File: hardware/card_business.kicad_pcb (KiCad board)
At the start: 2 copper layers, 49.9 x 17.3 mm, 12 parts, among them J1 Conn_01x01_Female, J2 USB_A, SW1 Reset, SW2 Boot, U1 CH552G

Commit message: Change pin name and routing update
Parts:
- SW1, SW2: footprint Connectors:C455281 -> Button_Switch_SMD:SW_SPST_TL3342
- moved R1 15.0 mm to (105.1, 95.5)
- moved R3 14.1 mm to (95.8, 92.8)
- moved SW1 13.2 mm to (114.1, 93.7), turned to 0 degrees
- moved D1 8.54 mm to (95.9, 88.0), turned to 180 degrees
- moved J2 6.96 mm to (79.5, 86.0)
- moved U1 6.13 mm to (104.2, 85.5)
- moved J1 5.32 mm to (136.5, 92.5)
- moved R2 5.28 mm to (111.1, 87.2)
- moved SW2 4.50 mm to (123.2, 93.7), turned to 0 degrees
- moved C1 3.46 mm to (98.0, 81.0)
- moved C2 3.25 mm to (98.0, 78.8)
- moved G*** 2.25 mm to (130.5, 81.0)
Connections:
- net /UDM renamed /UD-
- net /UDP renamed /UD+
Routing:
- net +5V: track 49.8 -> 64.0 mm, vias 2 -> 1
- net /PAD: track 27.0 -> 38.5 mm
- net GND: track 43.6 -> 33.2 mm, vias 2 -> 1
- net Net-(R2-Pad1): track 9.01 -> 17.9 mm
- net /RST: track 2.25 -> 10.9 mm
- net /UD-: track 24.9 -> 20.0 mm
- net /UD+: track 28.5 -> 30.2 mm, vias 3 -> 1
- net /P3.3: track 7.80 -> 6.74 mm
- net Net-(R1-Pad2): track 12.2 -> 11.3 mm
- net Net-(D1-Pad2): track 5.48 -> 4.78 mm
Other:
- board size 49.9 x 17.3 mm -> 62 x 22.5 mm

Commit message: update labels
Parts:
- renumbered SW2 to BOOT, D1 to LED, SW1 to RST, J1 to TOUCHME
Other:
- board text added: "Phone: 4491101599"
- board text removed: "Phone: XXXXXXXXXX"

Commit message: add back labels
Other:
- board text added: "Instructions: 1.- Plug into USB port 2.- Wait for device to be ready 3.- Open your favorite tex editor 4.- Press Caps Lock three times 5.- Watch the magic!"

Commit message: update traces v1.0
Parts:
- turned BOOT to 180 degrees
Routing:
- net Net-(R2-Pad1): track 17.9 -> 27.6 mm
- net +5V: track 64.0 -> 72.3 mm
- net Net-(D1-Pad2): track 4.78 -> 8.39 mm
- net /PAD: track 38.5 -> 39.2 mm
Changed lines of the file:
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@@
-(kicad_pcb (version 20171130) (host pcbnew "(5.1.9)-1")
+(kicad_pcb (version 20171130) (host pcbnew "(5.1.5-0-10_14)")
   (general
     (thickness 1.6)
     (drawings 21)
-    (tracks 100)
+    (tracks 112)
     (zones 0)
     (modules 12)
@@
   )
   (setup
-    (last_trace_width 0.25)
+    (last_trace_width 0.3)
+    (user_trace_width 0.3)
+    (user_trace_width 0.5)
     (trace_clearance 0.2)
     (zone_clearance 0.508)
@@
   )
   (module Button_Switch_SMD:SW_SPST_TL3342 (layer F.Cu)
-    (at 123.15 93.65)
+    (at 123.15 93.65 180)
     (descr "Low-profile SMD Tactile Switch, https://www.e-switch.com/system/asset/product_line/data_sheet/165/TL3342.pdf")
     (tags "SPST Tactile Switch")
@@
       (effects (font (size 1 1) (thickness 0.15)))
     )
-    (pad 2 smd rect (at 3.15 1.9) (size 1.7 1) (layers F.Cu F.Paste F.Mask)
+    (pad 2 smd rect (at 3.15 1.9 180) (size 1.7 1) (layers F.Cu F.Paste F.Mask)
       (net 1 +5V))
-    (pad 2 smd rect (at -3.15 1.9) (size 1.7 1) (layers F.Cu F.Paste F.Mask)
+    (pad 2 smd rect (at -3.15 1.9 180) (size 1.7 1) (layers F.Cu F.Paste F.Mask)
       (net 1 +5V))
-    (pad 1 smd rect (at 3.15 -1.9) (size 1.7 1) (layers F.Cu F.Paste F.Mask)
+    (pad 1 smd rect (at 3.15 -1.9 180) (size 1.7 1) (layers F.Cu F.Paste F.Mask)
       (net 7 "Net-(R2-Pad1)"))
-    (pad 1 smd rect (at -3.15 -1.9) (size 1.7 1) (layers F.Cu F.Paste F.Mask)
+    (pad 1 smd rect (at -3.15 -1.9 180) (size 1.7 1) (layers F.Cu F.Paste F.Mask)
       (net 7 "Net-(R2-Pad1)"))
     (model ${KISYS3DMOD}/Button_Switch_SMD.3dshapes/SW_SPST_TL3342.wrl
@@
     (effects (font (size 2 2) (thickness 0.3)))
   )
-  (segment (start 99 78.75) (end 99 81) (width 0.3) (layer B.Cu) (net 1))
   (segment (start 99 81) (end 99 82) (width 0.3) (layer B.Cu) (net 1))
   (segment (start 99.325 82.325) (end 101 82.325) (width 0.3) (layer B.Cu) (net 1))
   (segment (start 99 82) (end 99.325 82.325) (width 0.3) (layer B.Cu) (net 1))
-  (via (at 103.5 85) (size 0.8) (drill 0.4) (layers F.Cu B.Cu) (net 1))
-  (segment (start 103.5 84.025) (end 103.5 85) (width 0.3) (layer B.Cu) (net 1))
-  (segment (start 101.8 82.325) (end 103.5 84.025) (width 0.3) (layer B.Cu) (net 1))
-  (segment (start 101 82.325) (end 101.8 82.325) (width 0.3) (layer B.Cu) (net 1))
-  (segment (start 120 95.55) (end 119.55 95.55) (width 0.3) (layer F.Cu) (net 1))
-  (segment (start 126.3 95.55) (end 120 95.55) (width 0.3) (layer F.Cu) (net 1))
-  (segment (start 120 95.55) (end 120 94.5) (width 0.3) (layer F.Cu) (net 1))
-  (segment (start 120 94.5) (end 119.25 93.75) (width 0.3) (layer F.Cu) (net 1))
-  (segment (start 119.25 93.75) (end 117.75 93.75) (width 0.3) (layer F.Cu) (net 1))
-  (segment (start 117.25 93.25) (end 117.25 91.75) (width 0.3) (layer F.Cu) (net 1))
-  (segment (start 117.75 93.75) (end 117.25 93.25) (width 0.3) (layer F.Cu) (net 1))
-  (segment (start 117.25 91.75) (end 110.95 91.75) (width 0.3) (layer F.Cu) (net 1))
-  (segment (start 103.5 85) (end 103.5 90.5) (width 0.3) (layer F.Cu) (net 1))
-  (segment (start 104.75 91.75) (end 110.95 91.75) (width 0.3) (layer F.Cu) (net 1))
-  (segment (start 84.4 89.81) (end 92.31 89.81) (width 0.3) (layer F.Cu) (net 1))
-  (segment (start 92.31 89.81) (end 93 90.5) (width 0.3) (layer F.Cu) (net 1))
-  (segment (start 93 90.5) (end 93 91.75) (width 0.3) (layer F.Cu) (net 1))
-  (segment (start 93 91.75) (end 94 92.75) (width 0.3) (layer F.Cu) (net 1))
-  (segment (start 101.5 92.75) (end 103.625 90.625) (width 0.3) (layer F.Cu) (net 1))
-  (segment (start 94 92.75) (end 101.5 92.75) (width 0.3) (layer F.Cu) (net 1))
-  (segment (start 103.625 90.625) (end 104.75 91.75) (width 0.3) (layer F.Cu) (net 1))
-  (segment (start 103.5 90.5) (end 103.625 90.625) (width 0.3) (layer F.Cu) (net 1))
+  (segment (start 120 95.55) (end 119.55 95.55) (width 0.3) (layer F.Cu) (net 7))
+  (segment (start 99 81) (end 99 78.75) (width 0.5) (layer B.Cu) (net 1))
+  (via (at 103.71 78.6) (size 0.8) (drill 0.4) (layers F.Cu B.Cu) (net 1))
+  (segment (start 103.56 78.75) (end 103.71 78.6) (width 0.5) (layer B.Cu) (net 1))
+  (segment (start 99 78.75) (end 103.56 78.75) (width 0.5) (layer B.Cu) (net 1))
+  (segment (start 92.858 89.81) (end 84.4 89.81) (width 0.5) (layer F.Cu) (net 1))
+  (segment (start 94.798 91.75) (end 92.858 89.81) (width 0.5) (layer F.Cu) (net 1))
+  (segment (start 103.688 91.75) (end 103.71 91.728) (width 0.5) (layer F.Cu) (net 1))
+  (segment (start 103.71 90.7) (end 103.71 91) (width 0.5) (layer F.Cu) (net 1))
+  (segment (start 103.71 91) (end 102.94 91.77) (width 0.5) (layer F.Cu) (net 1))
+  (segment (start 103.688 91.75) (end 102.94 91.77) (width 0.5) (layer F.Cu) (net 1))
+  (segment (start 102.94 91.77) (end 94.798 91.75) (width 0.5) (layer F.Cu) (net 1))
+  (segment (start 103.71 90.7) (end 103.71 78.6) (width 0.5) (layer F.Cu) (net 1))
+  (segment (start 103.71 91.04) (end 103.71 91.26) (width 0.5) (layer F.Cu) (net 1))
+  (segment (start 104.22 91.77) (end 103.688 91.75) (width 0.5) (layer F.Cu) (net 1))
+  (segment (start 103.71 91.26) (end 104.22 91.77) (width 0.5) (layer F.Cu) (net 1))
+  (segment (start 103.71 91.728) (end 103.71 91.04) (width 0.5) (layer F.Cu) (net 1))
+  (segment (start 103.71 91.04) (end 103.71 90.7) (width 0.5) (layer F.Cu) (net 1))
+  (segment (start 104.477838 91.767838) (end 103.71 91) (width 0.5) (layer F.Cu) (net 1))
+  (segment (start 104.947838 91.767838) (end 104.477838 91.767838) (width 0.5) (layer F.Cu) (net 1))
+  (segment (start 110.95 91.75) (end 104.947838 91.767838) (width 0.5) (layer F.Cu) (net 1))
+  (segment (start 104.947838 91.767838) (end 104.22 91.77) (width 0.5) (layer F.Cu) (net 1))
+  (segment (start 117.25 91.75) (end 110.95 91.75) (width 0.5) (layer F.Cu) (net 1))
+  (segment (start 119.39999 91.75) (end 119.39999 91.998532) (width 0.5) (layer F.Cu) (net 1))
+  (segment (start 117.25 91.75) (end 119.39999 91.75) (width 0.5) (layer F.Cu) (net 1))
   (segment (start 97.1 78.75) (end 97.1 81) (width 0.3) (layer B.Cu) (net 2))
   (segment (start 97.1 81) (end 97.1 82.85) (width 0.3) (layer B.Cu) (net 2))
@@
   (segment (start 98 86.875) (end 98 82.75) (width 0.3) (layer F.Cu) (net 2))
   (segment (start 96.875 88) (end 98 86.875) (width 0.3) (layer F.Cu) (net 2))
-  (via (at 95 90.75) (size 0.8) (drill 0.4) (layers F.Cu B.Cu) (net 3))
-  (segment (start 94.925 90.825) (end 95 90.75) (width 0.3) (layer B.Cu) (net 3))
-  (segment (start 94.925 92.75) (end 94.925 90.825) (width 0.3) (layer B.Cu) (net 3))
-  (segment (start 95 90.75) (end 95 88) (width 0.3) (layer F.Cu) (net 3))
-  (via (at 135.75 82.75) (size 0.8) (drill 0.4) (layers F.Cu B.Cu) (net 4))
-  (segment (start 136.5 83.5) (end 135.75 82.75) (width 0.3) (layer F.Cu) (net 4))
-  (segment (start 136.5 92.5) (end 136.5 83.5) (width 0.3) (layer F.Cu) (net 4))
-  (segment (start 135.325 82.325) (end 107.5 82.325) (width 0.3) (layer B.Cu) (net 4))
-  (segment (start 135.75 82.75) (end 135.325 82.325) (width 0.3) (layer B.Cu) (net 4))
+  (via (at 93.01 87.95) (size 0.8) (drill 0.4) (layers F.Cu B.Cu) (net 3))
+  (segment (start 95 88) (end 93.06 88) (width 0.3) (layer F.Cu) (net 3))
+  (segment (start 93.06 88) (end 93.01 87.95) (width 0.3) (layer F.Cu) (net 3))
+  (segment (start 94.35 87.95) (end 93.01 87.95) (width 0.3) (layer B.Cu) (net 3))
+  (segment (start 94.925 88.525) (end 94.35 87.95) (width 0.3) (layer B.Cu) (net 3))
+  (segment (start 94.925 92.75) (end 94.925 88.525) (width 0.3) (layer B.Cu) (net 3))
   (segment (start 117.25 95.55) (end 110.95 95.55) (width 0.3) (layer F.Cu) (net 5))
   (via (at 108.5 95.5) (size 0.8) (drill 0.4) (layers F.Cu B.Cu) (net 5))
@@
   (segment (start 105.095 87.405) (end 107.5 87.405) (width 0.3) (layer B.Cu) (net 6))
   (segment (start 104.175 88.325) (end 105.095 87.405) (width 0.3) (layer B.Cu) (net 6))
-  (segment (start 126.3 91.75) (end 120 91.75) (width 0.3) (layer F.Cu) (net 7))
-  (via (at 118.75 87.5) (size 0.8) (drill 0.4) (layers F.Cu B.Cu) (net 7))
-  (segment (start 120 88.75) (end 118.75 87.5) (width 0.3) (layer F.Cu) (net 7))
-  (segment (start 120 91.75) (end 120 88.75) (width 0.3) (layer F.Cu) (net 7))
+  (segment (start 117.25 91.75) (end 120 91.75) (width 0.5) (layer F.Cu) (net 1))
+  (segment (start 121.35 91.75) (end 126.3 91.75) (width 0.5) (layer F.Cu) (net 1))
+  (segment (start 120 91.75) (end 121.35 91.75) (width 0.5) (layer F.Cu) (net 1))
+  (via (at 136.49 82.32) (size 0.8) (drill 0.4) (layers F.Cu B.Cu) (net 4))
+  (segment (start 136.485 82.325) (end 136.49 82.32) (width 0.3) (layer B.Cu) (net 4))
+  (segment (start 125.965 82.325) (end 136.485 82.325) (width 0.3) (layer B.Cu) (net 4))
+  (segment (start 125.965 82.325) (end 107.5 82.325) (width 0.3) (layer B.Cu) (net 4))
+  (segment (start 136.49 92.49) (end 136.5 92.5) (width 0.3) (layer F.Cu) (net 4))
+  (segment (start 136.49 82.32) (end 136.49 92.49) (width 0.3) (layer F.Cu) (net 4))
   (segment (start 112.25 87.5) (end 112 87.25) (width 0.3) (layer B.Cu) (net 7))
-  (segment (start 118.75 87.5) (end 112.25 87.5) (width 0.3) (layer B.Cu) (net 7))
+  (segment (start 126.3 95.55) (end 128.62 95.55) (width 0.3) (layer F.Cu) (net 7))
+  (segment (start 128.62 95.55) (end 129.32 94.85) (width 0.3) (layer F.Cu) (net 7))
+  (segment (start 115.87 87.5) (end 121.16 87.5) (width 0.3) (layer B.Cu) (net 7))
+  (segment (start 115.87 87.5) (end 112.25 87.5) (width 0.3) (layer B.Cu) (net 7))
+  (segment (start 121.16 87.5) (end 121.85 88.19) (width 0.3) (layer B.Cu) (net 7))
+  (via (at 121.85 95.45) (size 0.8) (drill 0.4) (layers F.Cu B.Cu) (net 7))
+  (segment (start 121.85 88.19) (end 121.85 95.45) (width 0.3) (layer B.Cu) (net 7))
+  (segment (start 121.85 95.45) (end 126.3 95.55) (width 0.5) (layer F.Cu) (net 7))
+  (segment (start 120 95.55) (end 121.85 95.45) (width 0.5) (layer F.Cu) (net 7))
   (segment (start 96.75 92.75) (end 97.5 92.75) (width 0.25) (layer B.Cu) (net 8))
   (segment (start 97.5 92.75) (end 99 91.25) (width 0.25) (layer B.Cu) (net 8))

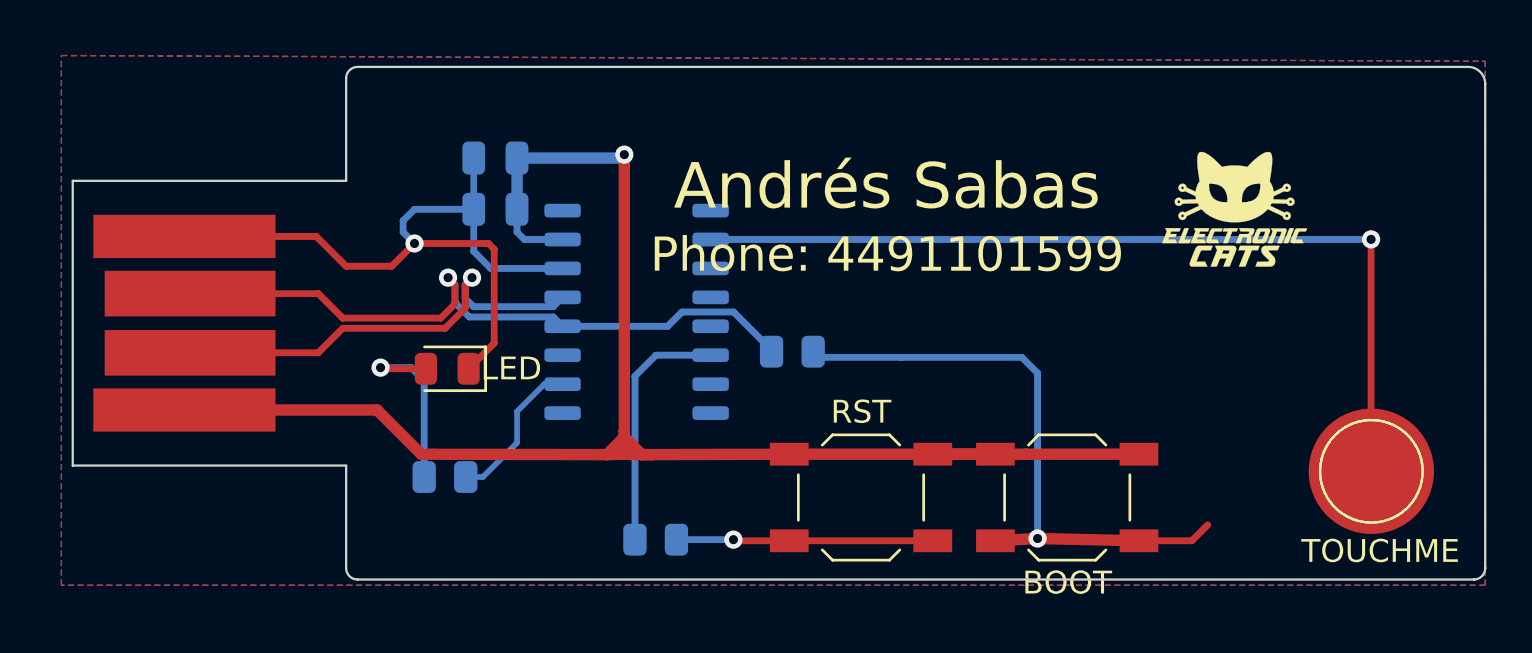
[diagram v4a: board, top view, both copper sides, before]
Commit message: add capacitor, modify traces
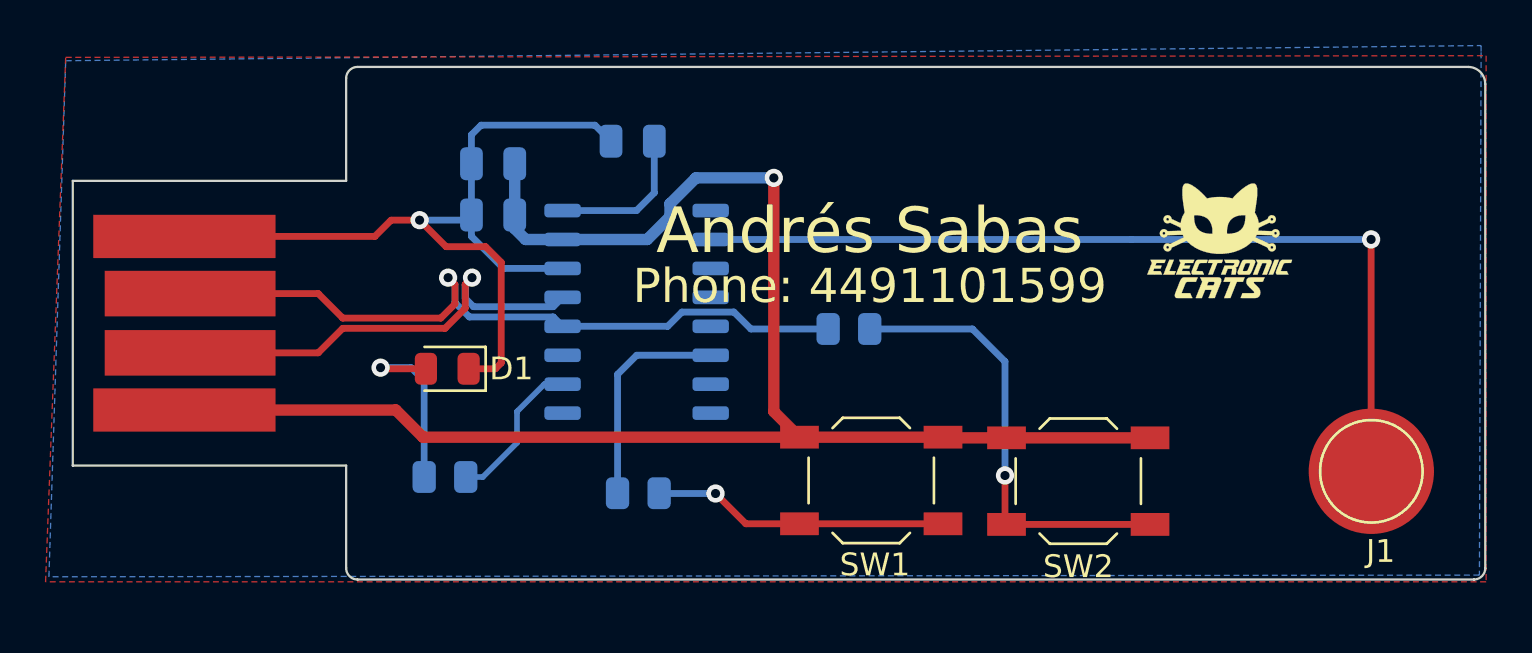
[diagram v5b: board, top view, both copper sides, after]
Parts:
- added C3: 0.1uF, Capacitor_SMD:C_0805_2012Metric, B.Cu at (104.1, 78.0)
- moved R2 2.67 mm to (113.6, 86.3)
- moved R1 2.18 mm to (104.3, 93.5)
- moved G*** 1.53 mm to (129.8, 82.4)
- moved SW1 0.87 mm to (114.5, 92.9)
- moved SW2 0.87 mm to (123.6, 92.9)
- moved C1 0.27 mm to (98.0, 81.2)
- moved C2 0.27 mm to (98.0, 79.0)
- renumbered LED to D1, TOUCHME to J1, RST to SW1, BOOT to SW2
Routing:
- net Net-(R2-Pad1): track 27.6 -> 20.0 mm
- net Net-(C3-Pad2): track 0.00 -> 6.61 mm
- net GND: track 33.2 -> 38.9 mm
- net /UD+: track 30.2 -> 32.2 mm
- net Net-(R1-Pad2): track 11.3 -> 13.0 mm
- net +5V: track 72.3 -> 70.6 mm
- net /RST: track 10.9 -> 9.65 mm
